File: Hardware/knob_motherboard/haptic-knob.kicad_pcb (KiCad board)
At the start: 4 copper layers, 50 x 50 mm, 74 parts, among them J1 USB_C_Receptacle_USB2.0, J2 Conn_01x14_Socket, J3 Conn_ARM_SWD_TagConnect_TC203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, M1 BLDC, U1 ESP32-S3-WROOM-1U, U2 PDRV8311HRRWR, U3 MT6701, U4 CH224K, U5 LSM6DSO, U6 MT2492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

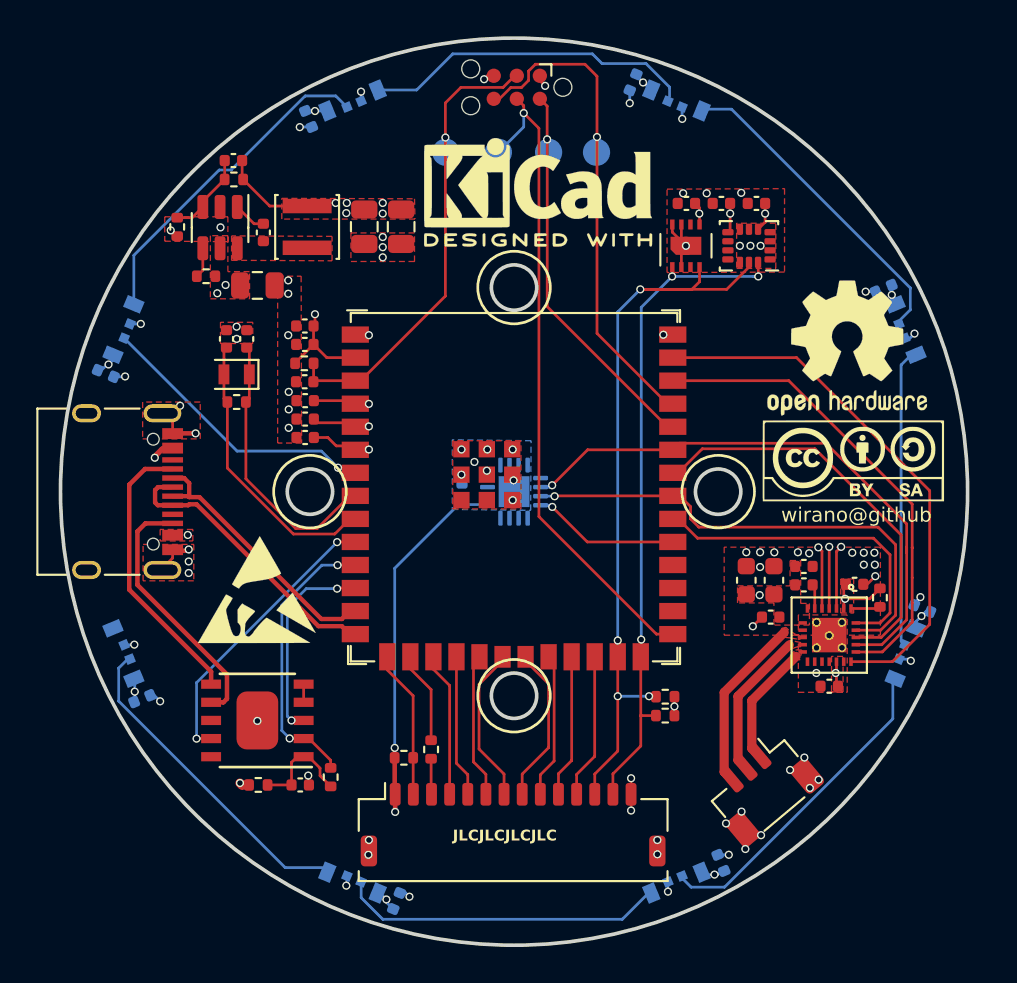
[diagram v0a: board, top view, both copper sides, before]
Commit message: CH224K & ST77903 symbol fix
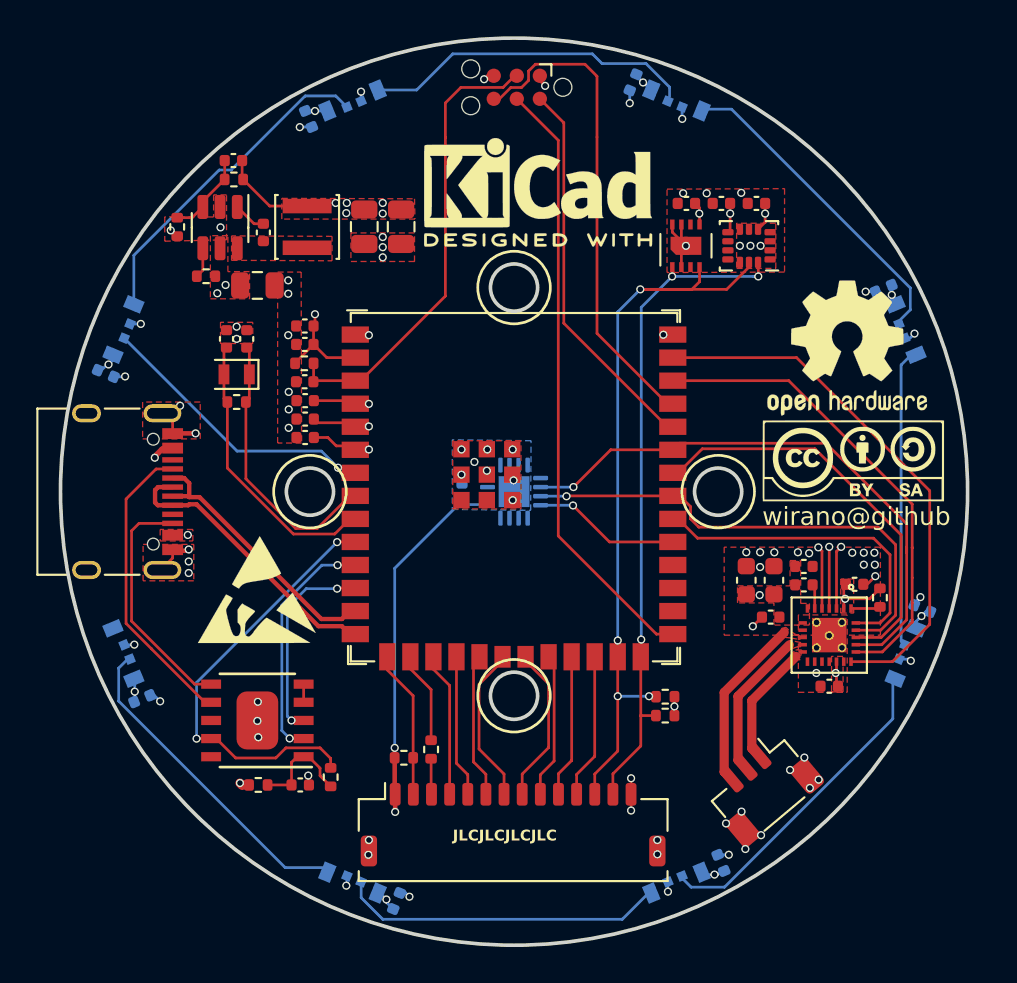
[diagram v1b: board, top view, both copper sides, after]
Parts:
- removed TP1, TP2, TP3, TP4: TestPoint, TestPoint:TestPoint_Pad_D1.5mm
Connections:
- U1 pad 10: /Core/CFG3 -> /Core/CFG1
- U1 pad 11: /Core/CFG1 -> /Core/CFG2
- U1 pad 12: /Core/CFG2 -> /Core/CFG3
- U4 pad 2: /Core/CFG1 -> /Core/CFG2
- U4 pad 3: /Core/CFG2 -> /Core/CFG3
- U4 pad 6: Net-(J1-CC1) -> Net-(J1-CC2)
- U4 pad 7: Net-(J1-CC2) -> Net-(J1-CC1)
- U4 pad 9: /Core/CFG3 -> /Core/CFG1
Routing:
- net /Core/CFG1: track 15.7 -> 23.9 mm
- net /Core/CFG3: track 15.9 -> 11.5 mm
- net /Core/BOOT: track 36.3 -> 33.6 mm, vias 1 -> 0
- net /Core/CFG2: track 11.5 -> 13.6 mm
- net Net-(J1-CC2): track 14.3 -> 13.2 mm
- net Net-(J1-CC1): track 15.6 -> 16.6 mm
- net /Core/RXD: vias 1 -> 0
- net GND: vias 82 -> 84
- net /Core/nRST: vias 1 -> 0
- net /Core/TXD: vias 1 -> 0
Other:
- outline, holes or cut-outs redrawn
